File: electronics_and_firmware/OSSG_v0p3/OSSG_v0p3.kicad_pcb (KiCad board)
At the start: 4 copper layers, 85 x 9 mm, 77 parts, among them IC1 DW01A, J1 USB_B_Micro, J2 External PDM Mic Input, Q1 FS8205A, Q2 Q_NPN_BEC, Q3 Q_NPN_BEC, SW1 SW_SPST, U1 ESP32-PICO-D4, U2 TP4056, U3 XC6222B331MRG, U4 FT232RQ, U5 APX803L-29SA-7, U6 MP23DB01HPTR

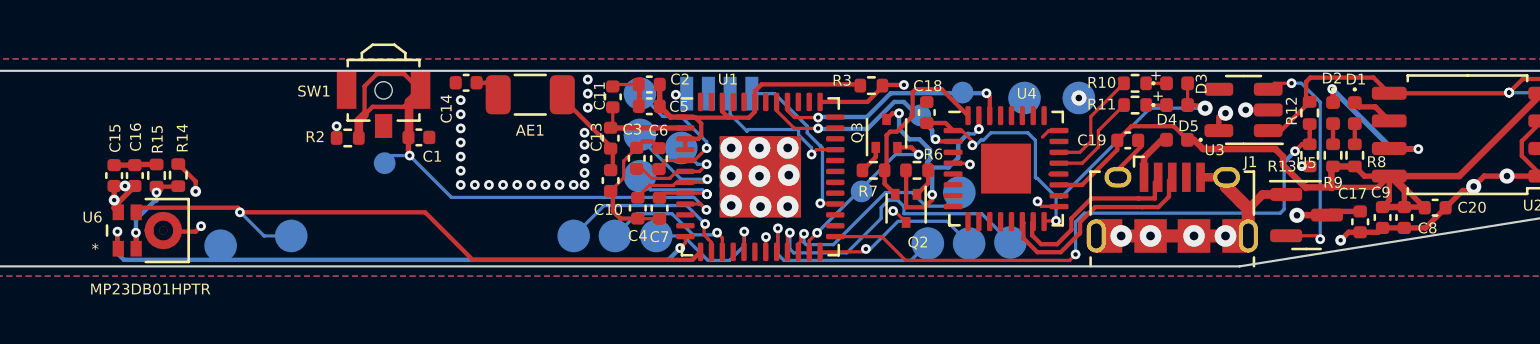
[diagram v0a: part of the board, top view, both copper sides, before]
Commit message: add in part numbers and prices for almost all components for LCSC
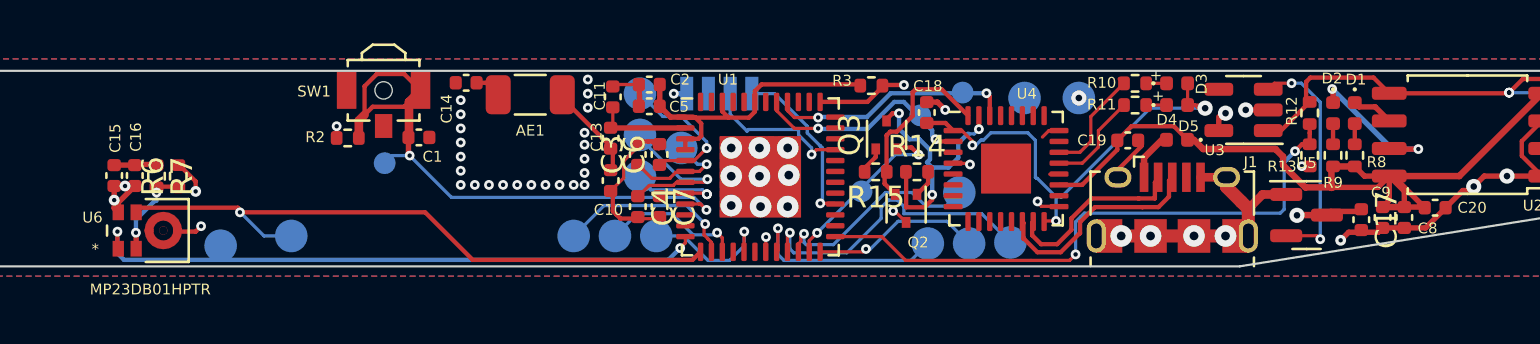
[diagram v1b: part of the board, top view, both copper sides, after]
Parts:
- C13: value NC -> NC_0R
- R14, R15: value 10K* -> 10K
- R6, R7: value 10K -> 10K*
- moved R6 34.0 mm to (86.2, 79.8), turned to 90 degrees
- moved R14 34.0 mm to (120.2, 79.7), turned to 0 degrees
- moved R15 33.1 mm to (118.2, 79.7), turned to 180 degrees
- moved R7 33.0 mm to (85.2, 79.8), turned to -90 degrees
- moved C6 0.19 mm to (108.3, 78.8), turned to 90 degrees
- moved C3 0.18 mm to (107.3, 78.8), turned to 90 degrees
- moved C17 0.11 mm to (140.6, 81.8)
- moved C7 0.08 mm to (108.3, 81.2), turned to -90 degrees
- moved Q3 0.07 mm to (118.8, 78.0)
- moved C4 0.07 mm to (107.3, 81.2), turned to -90 degrees
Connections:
- C3 pad 1: GND -> ADC1C0
- C3 pad 2: ADC1C0 -> GND
- C4 pad 1: GND -> ADC1C1
- C4 pad 2: ADC1C1 -> GND
- C6 pad 1: GND -> ADC1C2
- C6 pad 2: ADC1C2 -> GND
- C7 pad 1: GND -> ADC1C3
- C7 pad 2: ADC1C3 -> GND
- R14 pad 1: +3V3 -> DTR
- R14 pad 2: Net-(R14-Pad2) -> Net-(Q2-Pad1)
- R15 pad 1: Net-(R14-Pad2) -> RTS
- R15 pad 2: GND -> Net-(Q3-Pad1)
- R6 pad 1: DTR -> Net-(U6-Pad2)
- R6 pad 2: Net-(Q2-Pad1) -> +3V3
- R7 pad 1: RTS -> GND
- R7 pad 2: Net-(Q3-Pad1) -> Net-(U6-Pad2)
- U6 pad 2: Net-(R14-Pad2) -> Net-(U6-Pad2)
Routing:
- net Net-(U6-Pad2): track 0.00 -> 4.32 mm, vias 0 -> 2
- net Net-(R14-Pad2): track 4.32 -> 0.00 mm, vias 2 -> 0
- net GND: track 49.0 -> 50.0 mm, vias 45 -> 46
- added copper zone on In2.Cu, net GND

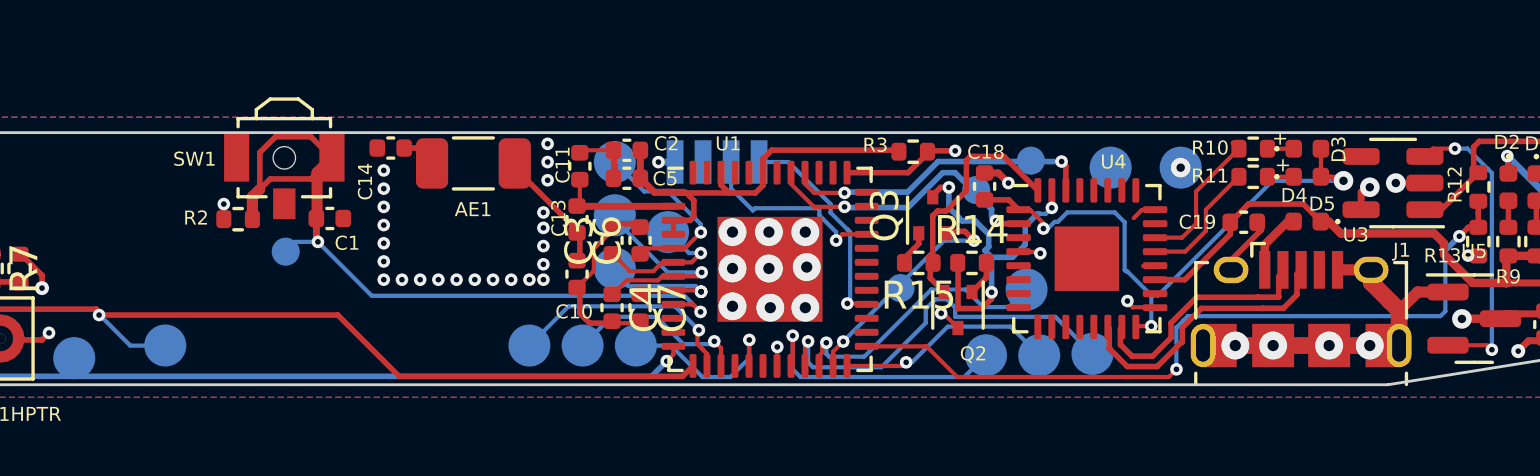
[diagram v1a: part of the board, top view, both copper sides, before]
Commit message: switch from FT232 to CH99102F in schematic
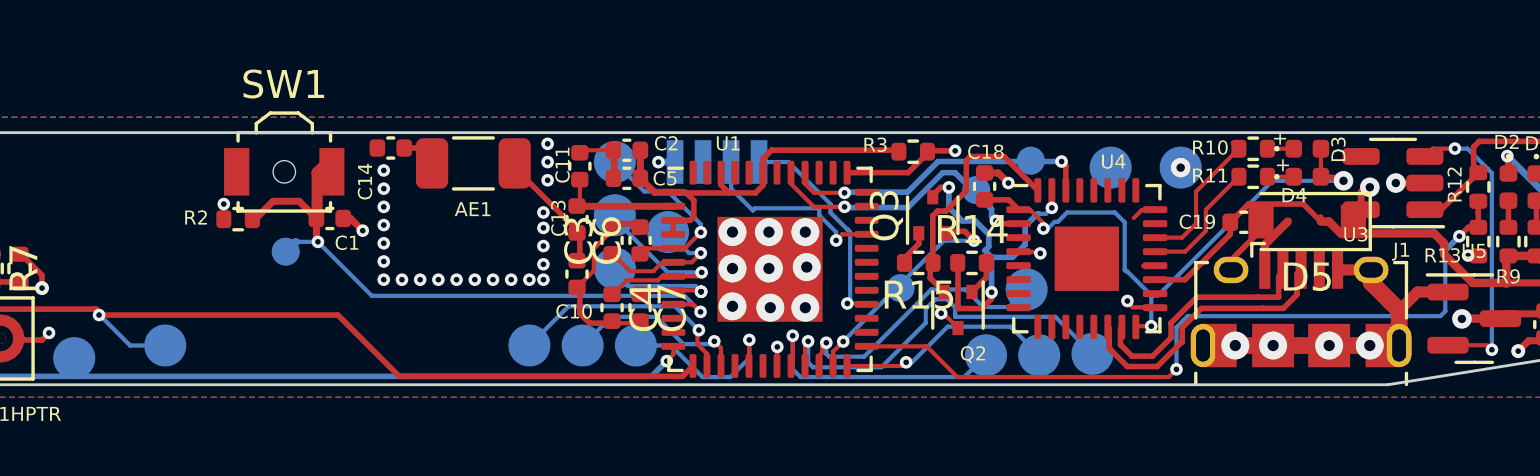
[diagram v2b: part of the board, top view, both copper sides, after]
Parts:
- D5: footprint Diode_SMD:D_0402_1005Metric -> Diode_SMD:D_SOD-123
- SW1: footprint Button_Switch_SMD:SW_SPST_B3U-3100P-B -> Button_Switch_SMD:SW_SPST_B3U-3000P-B
- moved SW1 0.32 mm to (95.6, 76.4)
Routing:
- net VCC_IN: track 38.4 -> 44.7 mm, vias 0 -> 1
- net EN: track 40.8 -> 35.7 mm
- net Net-(D5-Pad2): track 2.07 -> 0.00 mm
- net +3V3: track 16.1 -> 14.2 mm, vias 10 -> 9
- net GND: track 50.0 -> 48.6 mm, vias 46 -> 47

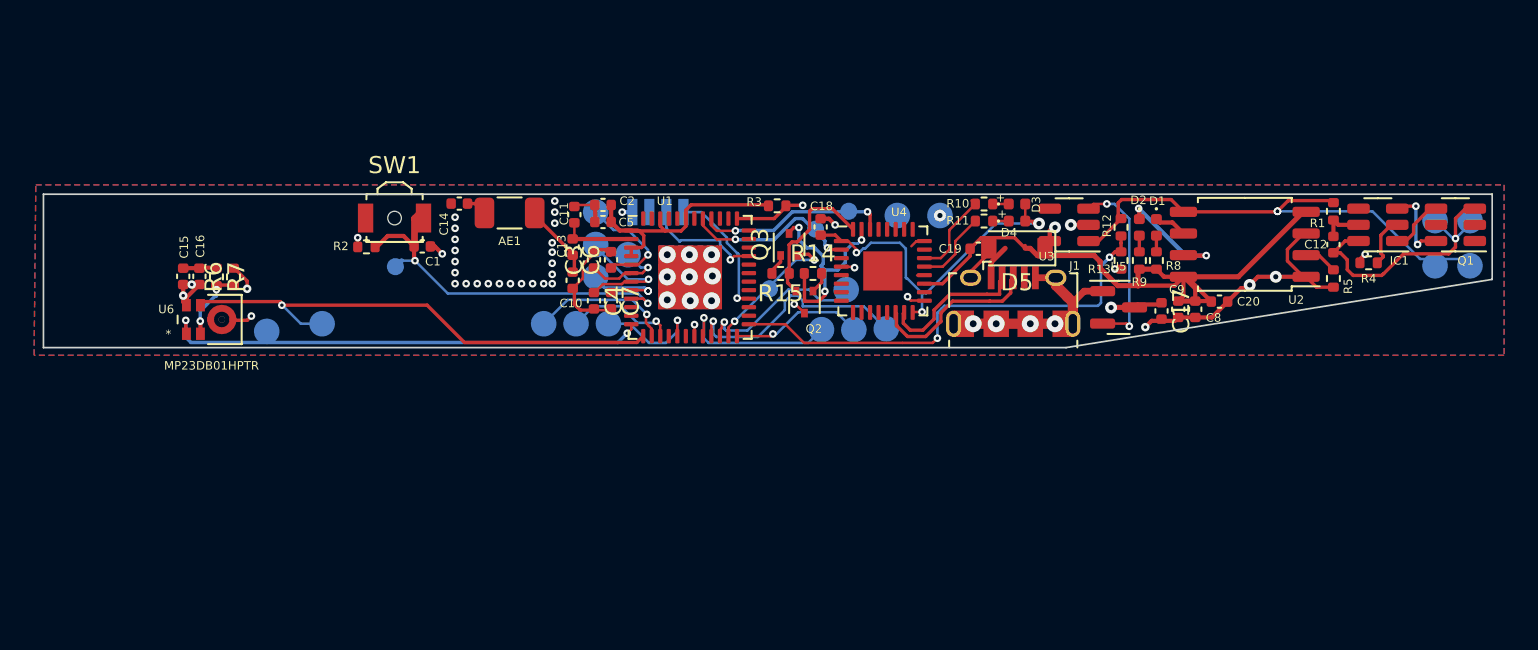
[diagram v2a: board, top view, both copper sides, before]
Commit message: add power supply switching, update all footprint to be accurate, move antenna to LCSC part, start new layout
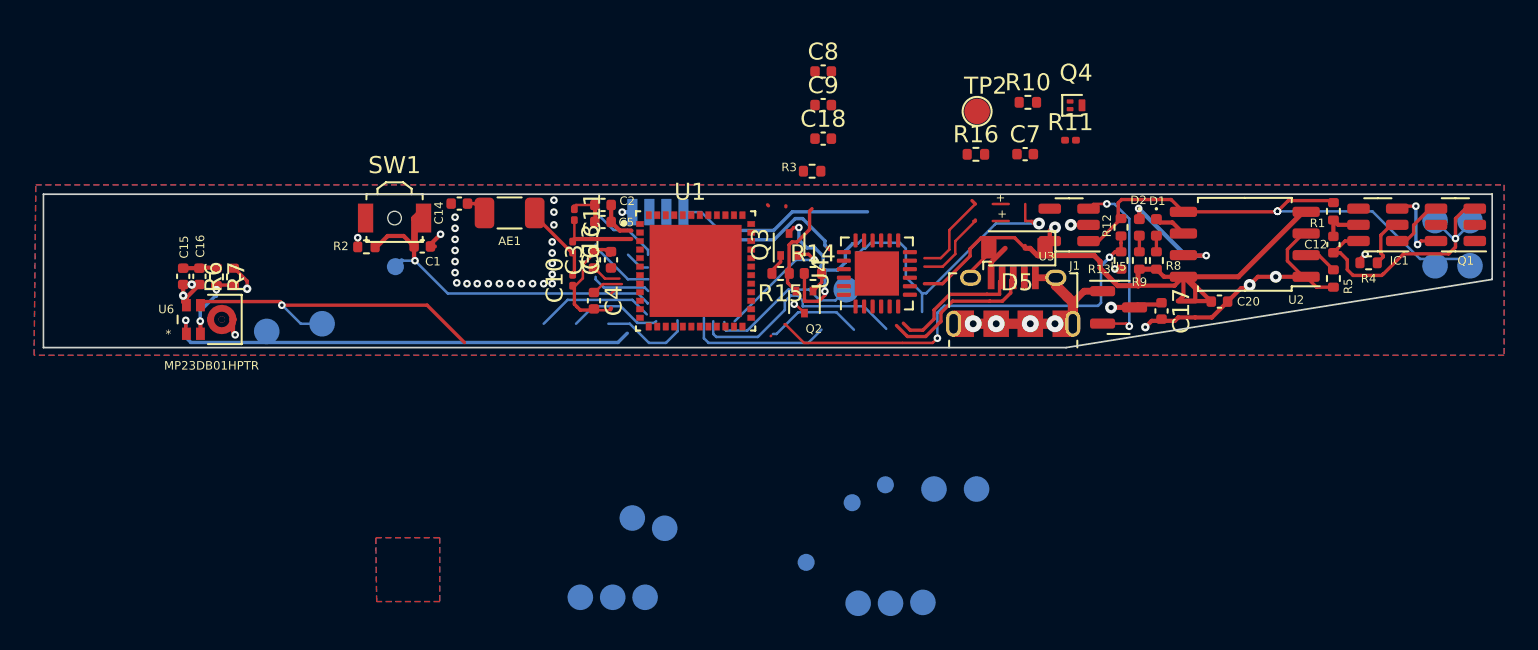
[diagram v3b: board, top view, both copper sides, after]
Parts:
- removed C19: 0.1uF, Capacitor_SMD:C_0402_1005Metric
- removed D3: TX, Diode_SMD:D_0402_1005Metric
- removed D4: RX, Diode_SMD:D_0402_1005Metric
- removed TP12: IO39_ADC1C3, OpenSourceSmartGlasses:BreakoutPadSmall
- added Q4: Q_PMOS_DGS, Package_TO_SOT_SMD:SOT-883, F.Cu at (135.6, 69.8)
- added R16: 100k, Resistor_SMD:R_0402_1005Metric, F.Cu at (129.7, 72.7)
- AE1: value H2U34W1H1Z0400 -> ANT3216LL00R2400A
- C10, C11, C13: footprint Capacitor_SMD:C_0402_1005Metric -> Capacitor_SMD:C_0201_0603Metric
- C7: value 0.1uF -> 1uF
- C8: value 4.7uF -> 1uF
- C9: value 10nF -> 0.1uF
- R10: value 270R -> 100k
- R11: value 270R -> NC; footprint Resistor_SMD:R_0402_1005Metric -> Resistor_SMD:R_0201_0603Metric
- R8, R9: value 330R -> 1k
- TP1, TP10, TP11, TP13, TP14, TP15, TP16, TP17, TP18, TP19, TP24, TP5, TP6, TP7: footprint OpenSourceSmartGlasses:BreakoutPadSmall -> OSSG_footprints:Breakout_pads
- TP2: value IO36_ADC1C2 -> IO12_SPI2_MISO; footprint OpenSourceSmartGlasses:BreakoutPadSmall -> OSSG_footprints:Breakout_pads; moved to F.Cu
- TP20: value IO15_SPI2_SCLK -> IO14_SPI2_SCLK; footprint OpenSourceSmartGlasses:BreakoutPadSmall -> OSSG_footprints:Breakout_pads
- TP21: value IO15_SPI2_MOSI -> IO13_SPI2_MOSI; footprint OpenSourceSmartGlasses:BreakoutPadSmall -> OSSG_footprints:Breakout_pads
- TP22: value IO23_BO -> IO32_BO; footprint OpenSourceSmartGlasses:BreakoutPadSmall -> OSSG_footprints:Breakout_pads
- U1: footprint OpenSourceSmartGlasses:ESP32_PICO_D4_smallGND -> OSSG_footprints:ESP32_PICO_D4
- U4: value FT232RQ -> CH9102F; footprint OpenSourceSmartGlasses:QFN32_5mmx5mm_smallEP -> Package_DFN_QFN:QFN-24-1EP_4x4mm_P0.5mm_EP2.6x2.6mm
- U5: value APX803L-29SA-7 -> CL7809SS
- moved C8 25.9 mm to (120.8, 67.8), turned to 0 degrees
- moved C7 25.8 mm to (132.6, 72.7), turned to 0 degrees
- moved C9 24.0 mm to (120.8, 69.8), turned to 0 degrees
- moved TP2 23.1 mm to (129.8, 70.1), turned to 0 degrees
- moved TP6 16.2 mm to (106.5, 98.7)
- moved TP7 16.2 mm to (108.4, 98.7)
- moved TP20 16.2 mm to (110.3, 98.7)
- moved TP1 16.2 mm to (124.7, 99.0)
- moved TP10 16.2 mm to (111.5, 94.6)
- moved TP17 16.2 mm to (129.8, 92.3)
- moved TP18 16.2 mm to (127.2, 92.3)
- moved TP3 16.2 mm to (122.5, 93.1)
- moved TP4 16.2 mm to (124.4, 92.0)
- moved TP9 16.2 mm to (119.8, 96.6)
- moved TP11 16.2 mm to (109.5, 94.0)
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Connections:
- C17 pad 1: +3V3 -> BATT+
- C18 pad 1: VCCIO -> +3V3
- C20 pad 1: VCC_IN -> V_USB
- C7 pad 1: ADC1C3 -> GND
- C7 pad 2: GND -> V_PSU
- C8 pad 1: VCC_IN -> GND
- C8 pad 2: GND -> VCC_IN
- C9 pad 1: VCC_IN -> Net-(C9-Pad1)
- D5 pad 1: VCC_IN -> V_PSU
- D5 pad 2: Net-(D5-Pad2) -> V_USB
- J1 pad 1: Net-(D5-Pad2) -> V_USB
- Q3 pad 2: IO0 -> DTR
- Q3 pad 3: DTR -> IO0
- R10 pad 1: Net-(R10-Pad1) -> GND
- R10 pad 2: Net-(D3-Pad1) -> PSEN
- R11 pad 1: Net-(R11-Pad1) -> PSEN
- R11 pad 2: Net-(D4-Pad1) -> V_PSU
- R12 pad 2: IO16 -> ADC1C2
- R13 pad 1: IO16 -> ADC1C2
- R8 pad 1: VCC_IN -> V_USB
- R9 pad 1: VCC_IN -> V_USB
- TP2 pad 1: ADC1C2 -> IO13
- U1 pad 8: ADC1C3 -> IO39
- U2 pad 4: VCC_IN -> V_USB
- U2 pad 8: VCC_IN -> V_USB
- U3 pad 1: BATT+ -> V_PSU
- U4 pad 1: VCCIO -> unconnected-(U4-Pad1)
- U4 pad 12: (no net) -> unconnected-(U4-Pad12)
- U4 pad 13: (no net) -> unconnected-(U4-Pad13)
- U4 pad 14: USB+ -> unconnected-(U4-Pad14)
- U4 pad 15: USB- -> unconnected-(U4-Pad15)
- U4 pad 16: VCCIO -> unconnected-(U4-Pad16)
- U4 pad 17: GND -> unconnected-(U4-Pad17)
- U4 pad 19: VCC_IN -> RTS
- U4 pad 2: TX_ESP -> GND
- U4 pad 20: GND -> TX_ESP
- U4 pad 21: Net-(R11-Pad1) -> RX_ESP
- U4 pad 22: Net-(R10-Pad1) -> unconnected-(U4-Pad22)
- U4 pad 23: (no net) -> DTR
- U4 pad 24: GND -> unconnected-(U4-Pad24)
- U4 pad 25: (no net) -> GND
- U4 pad 3: unconnected-(U4-Pad3) -> USB+
- U4 pad 4: GND -> USB-
- U4 pad 5: (no net) -> +3V3
- U4 pad 6: unconnected-(U4-Pad6) -> Net-(C9-Pad1)
- U4 pad 7: unconnected-(U4-Pad7) -> VCC_IN
- U4 pad 8: CTS -> VCC_IN
- U5 pad 3: +3V3 -> BATT+
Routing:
- net V_USB: track 0.00 -> 44.7 mm, vias 0 -> 1
- net VCC_IN: track 44.7 -> 0.00 mm, vias 1 -> 0
- net IO16: track 27.6 -> 0.00 mm, vias 2 -> 0
- net ADC1C2: track 6.96 -> 30.3 mm, vias 1 -> 2
- net VCCIO: track 21.3 -> 0.00 mm, vias 3 -> 0
- net (no net): track 0.00 -> 15.7 mm
- net +3.3VA: track 15.4 -> 2.54 mm
- net IO33: track 30.2 -> 19.5 mm
- net +3V3: track 14.2 -> 24.8 mm, vias 9 -> 6
- net IO0: track 8.33 -> 0.00 mm, vias 2 -> 0
- net DTR: track 12.8 -> 19.5 mm
- net ADC1C3: track 5.80 -> 0.00 mm, vias 2 -> 0
- net Net-(R10-Pad1): track 5.26 -> 0.00 mm
- net Net-(R11-Pad1): track 4.73 -> 0.00 mm
- net GND: track 48.6 -> 44.4 mm, vias 47 -> 35
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
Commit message: layout complete after fixing footprints, adding PSU switching, spreading out breakout points, etc.
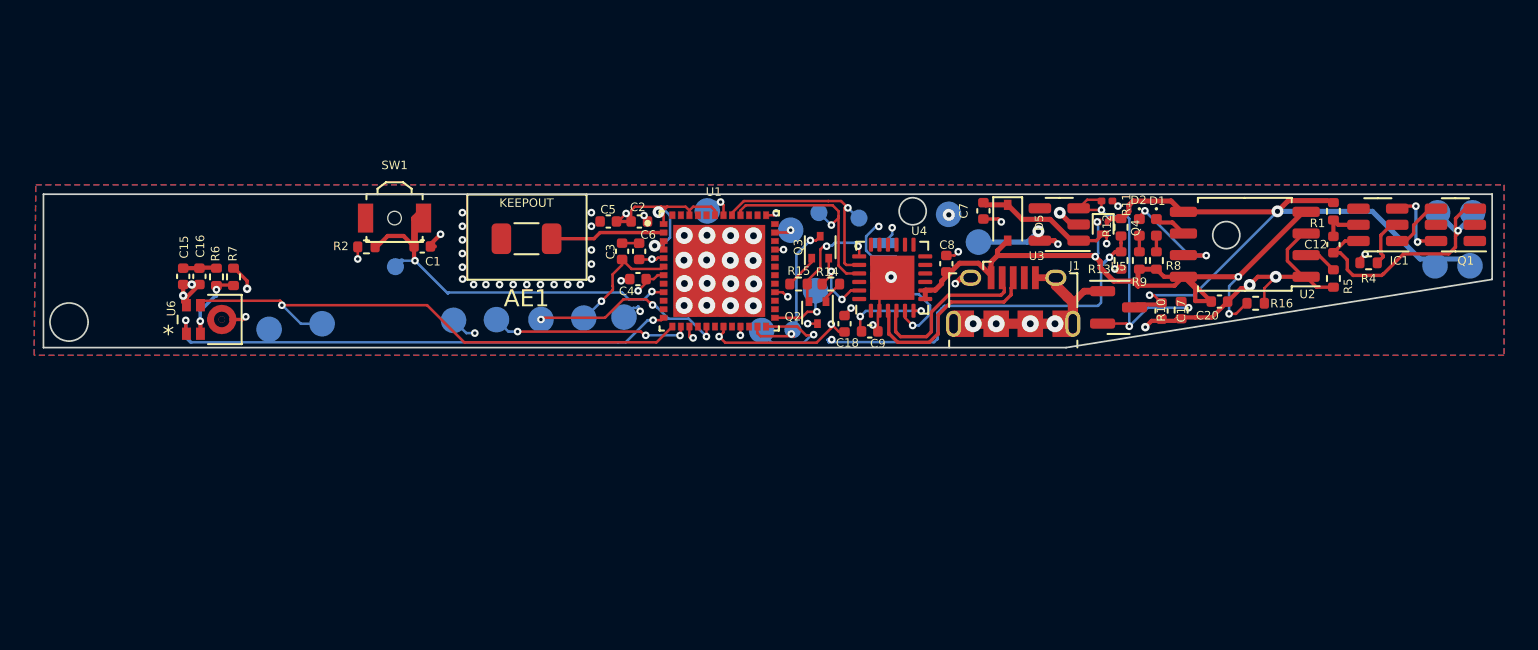
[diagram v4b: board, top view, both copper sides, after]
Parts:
- removed C10, C11: NC, Capacitor_SMD:C_0201_0603Metric
- removed C13: NC_0R, Capacitor_SMD:C_0201_0603Metric
- removed C14: Fine Tuning, Capacitor_SMD:C_0402_1005Metric
- removed R3: 0R, Resistor_SMD:R_0402_1005Metric
- removed TP5: IO2_Touch2, OSSG_footprints:Breakout_pads
- AE1: footprint Capacitor_SMD:C_1206_3216Metric -> OSSG_footprints:ANT3216LL00R2400A
- D5: footprint Diode_SMD:D_SOD-123 -> Diode_SMD:D_SOD-323
- J2: footprint footprints:Solder-4P-Connector -> OSSG_footprints:Solder-4P-Connector
- TP1: value IO4_Touch0 -> IO4_BO
- TP13: value L_Pos_Battery_Terminal -> +LBatt
- TP14: value L_Neg_Battery_Terminal -> -LBatt
- TP15: value R_Pos_Battery_Terminal -> +RBatt
- TP16: value R_Neg_Battery_Terminal -> -RBatt
- TP17: value +3.3V_Breakout -> +3.3V_BO
- TP18: value GND_Breakout -> GND_BO
- TP19: value IO15_SPI2_CS -> IO21_BO
- TP2: value IO12_SPI2_MISO -> IO18_BO; moved to B.Cu
- TP20: value IO14_SPI2_SCLK -> IO14_BO
- TP21: value IO13_SPI2_MOSI -> IO16_BO
- TP6: value IO25_DAC1 -> IO25_BO
- TP7: value IO26_DAC2 -> IO26_BO
- U6: value MP23DB01HPTR -> CHIP_B02MM_STM; footprint footprints:MP23DB01HPTR -> OSSG_footprints:MP23DB01HPTR
- moved TP19 26.2 mm to (114.0, 76.0)
- moved TP7 18.7 mm to (99.1, 82.4)
- moved R16 18.6 mm to (146.1, 81.4), turned to 180 degrees
- moved TP21 18.5 mm to (120.3, 80.7)
- moved TP1 17.7 mm to (117.1, 83.0)
- moved TP20 17.4 mm to (104.2, 82.3)
- moved TP6 17.0 mm to (101.6, 82.4)
- moved TP3 16.7 mm to (122.8, 76.4)
- moved TP4 16.4 mm to (120.5, 76.1)
- moved TP18 16.1 mm to (128.1, 76.2)
- moved R10 15.1 mm to (141.8, 81.8), turned to 90 degrees
- moved TP17 14.5 mm to (129.9, 77.8)
- moved J2 13.7 mm to (124.3, 79.4), turned to 90 degrees
- moved TP9 13.7 mm to (119.0, 83.0)
- moved C9 13.6 mm to (123.5, 83.0)
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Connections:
- AE1 pad 1: Net-(AE1-Pad1) -> unconnected-(AE1-Pad1)
- AE1 pad 2: Net-(AE1-Pad2) -> Net-(U1-Pad2)
- C8 pad 2: VCC_IN -> V_USB
- TP19 pad 1: IO15 -> IO21
- TP2 pad 1: IO13 -> IO18
- TP21 pad 1: IO13 -> IO16
- U1 pad 2: Net-(C11-Pad2) -> Net-(U1-Pad2)
- U4 pad 7: VCC_IN -> V_USB
- U4 pad 8: VCC_IN -> V_USB
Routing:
- net (no net): track 15.7 -> 0.00 mm
- net DTR: track 19.5 -> 4.95 mm, vias 3 -> 2
- net IO33: track 19.5 -> 32.1 mm
- net IO15: track 13.3 -> 0.68 mm, vias 0 -> 1
- net +3.3VA: track 2.54 -> 15.0 mm, vias 0 -> 3
- net V_PSU: track 0.00 -> 11.8 mm, vias 0 -> 2
- net ADC1C2: track 30.3 -> 41.3 mm, vias 2 -> 3
- net IO26: track 5.57 -> 15.9 mm, vias 0 -> 2
- net IO2: track 9.10 -> 0.00 mm
- net IO0: track 0.00 -> 8.99 mm, vias 0 -> 2
- net IO13: track 8.54 -> 0.00 mm
- net BATT+: track 31.8 -> 38.8 mm, vias 3 -> 2
- net Net-(U1-Pad2): track 0.00 -> 6.72 mm
- net PSEN: track 11.3 -> 17.9 mm, vias 2 -> 3
- net IO14: track 5.45 -> 12.0 mm, vias 0 -> 3
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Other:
- outline, holes or cut-outs redrawn
- board text added: "Design: Cayden Pierce, Nicholas Gray, Paul Hamilton"
- board text added: "Open Source Smart Glasses v0.3"
- board text added: "TeamOpenSmartGlasses"
- board text removed: "+"
